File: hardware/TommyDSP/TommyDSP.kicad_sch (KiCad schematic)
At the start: 7 parts

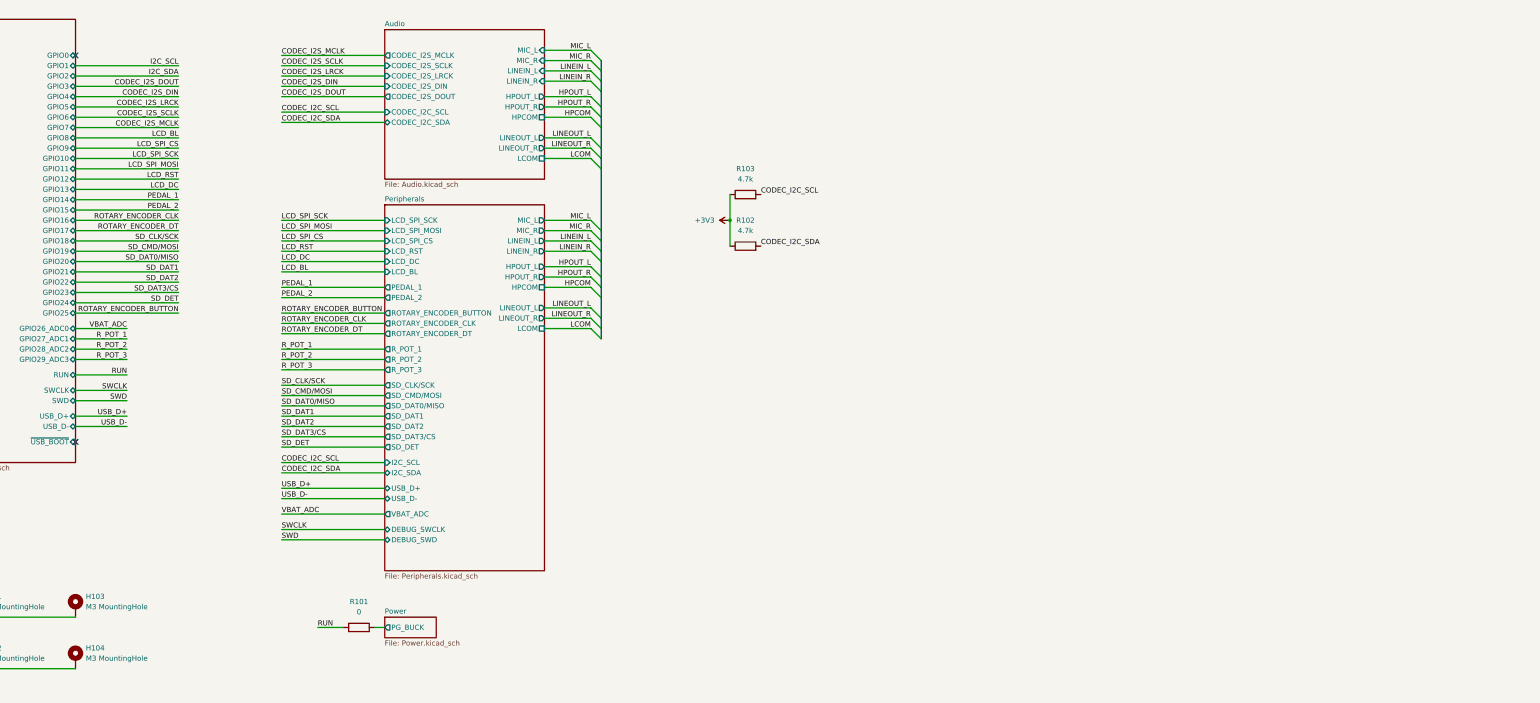
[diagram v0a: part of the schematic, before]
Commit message: bump to KiCad V10, add logo
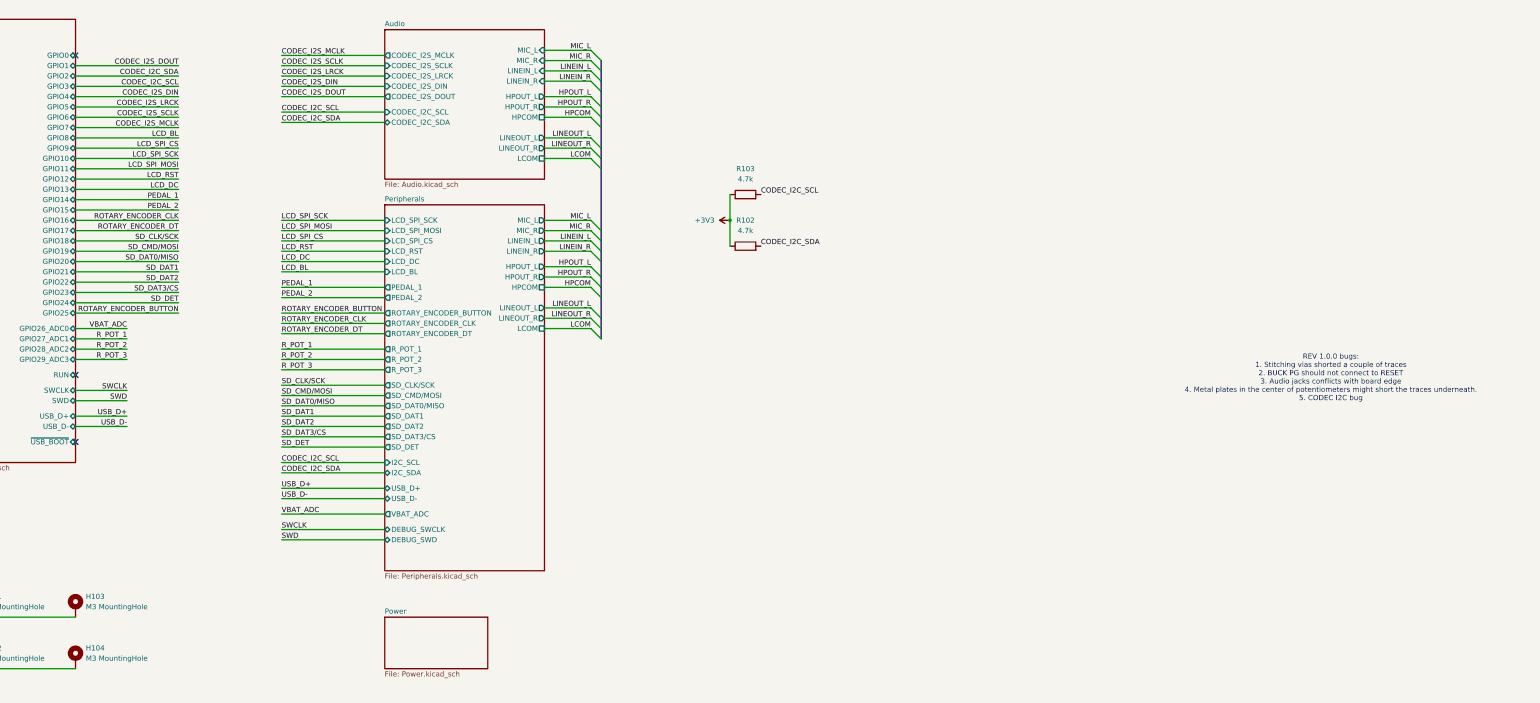
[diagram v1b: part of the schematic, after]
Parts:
- removed R101: 0, Resistor_SMD:R_0603_1608Metric, symbol Device:R
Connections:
- no-connect marks 2 -> 3
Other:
- sheet Power ports: added none; removed PG_BUCK
- note added: "REV 1.0.0 bugs: 1. Stitching vias shorted a couple of traces 2. BUCK PG should not connect to RESET 3. Audio jacks conflicts with board edge 4. Metal plates in the center of potentiometers might short the traces underneath. 5. CODEC I2C bug"
